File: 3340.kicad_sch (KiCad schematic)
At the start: 176 parts, among them J1 Conn_01x17, J10 FM1, J11 Conn_01x17, J12 V/OCT2, J13 PULSE2, J14 SAW2, J15 TRI2, J16 SINE2, J17 SYNC2, J18 Conn_01x17, J19 PWM2, J2 Conn_01x17, J20 FM2, J3 V/OCT1, J4 PULSE1, J5 SAW1, J6 TRI1, J7 SINE1, J8 SYNC1, J9 PWM1, Q1 2N3904, Q2 2N3906, Q3 2N3904, Q4 2N3906, Q5 2N3904, Q6 2N3904, SW2 DPDT_OOO, U1 TL072, U2 TL074, U3 CEM3340, U4 TL072, U5 CEM3340, U6 TL074

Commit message: Fix electrolytic footprints
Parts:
- C14, C15: footprint Capacitor_THT:C_Disc_D4.3mm_W1.9mm_P5.00mm -> Capacitor_THT:CP_Radial_D5.0mm_P2.00mm
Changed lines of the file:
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@@
       (effects (font (size 1.27 1.27)) (justify left))
     )
-    (property "Footprint" "Capacitor_THT:C_Disc_D4.3mm_W1.9mm_P5.00mm" (id 2) (at 61.9252 154.94 0)
+    (property "Footprint" "Capacitor_THT:CP_Radial_D5.0mm_P2.00mm" (id 2) (at 61.9252 154.94 0)
       (effects (font (size 1.27 1.27)) hide)
     )
@@
       (effects (font (size 1.27 1.27)) (justify left))
     )
-    (property "Footprint" "Capacitor_THT:C_Disc_D4.3mm_W1.9mm_P5.00mm" (id 2) (at 61.9252 172.72 0)
+    (property "Footprint" "Capacitor_THT:CP_Radial_D5.0mm_P2.00mm" (id 2) (at 61.9252 172.72 0)
       (effects (font (size 1.27 1.27)) hide)
     )
@@
     )
     (path "/4c10e0c8-c190-49b5-afef-1cfbf2c04b94"
-      (reference "C14") (unit 1) (value "10u") (footprint "Capacitor_THT:C_Disc_D4.3mm_W1.9mm_P5.00mm")
+      (reference "C14") (unit 1) (value "10u") (footprint "Capacitor_THT:CP_Radial_D5.0mm_P2.00mm")
     )
     (path "/575f3bf2-02c8-4aae-8013-f1397d2b5c57"
-      (reference "C15") (unit 1) (value "10u") (footprint "Capacitor_THT:C_Disc_D4.3mm_W1.9mm_P5.00mm")
+      (reference "C15") (unit 1) (value "10u") (footprint "Capacitor_THT:CP_Radial_D5.0mm_P2.00mm")
     )
     (path "/3a96b081-72fd-49bc-b6d2-c7dcd534bda7"

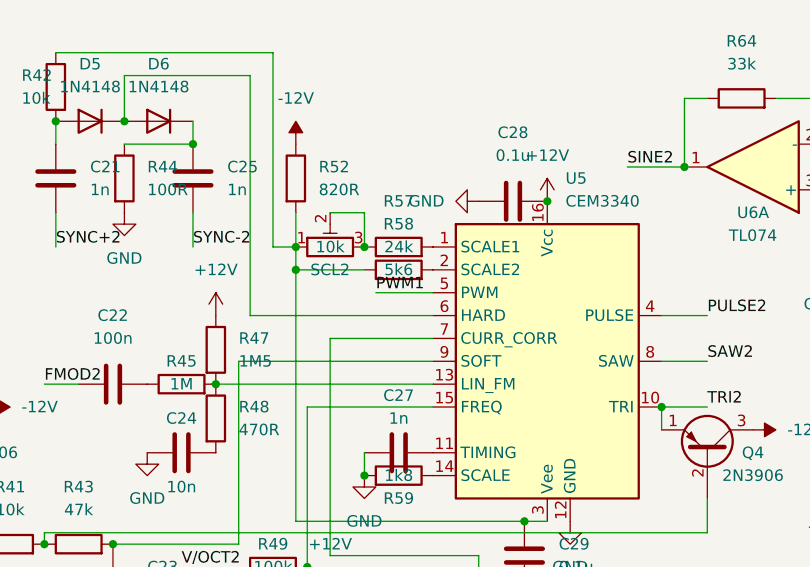
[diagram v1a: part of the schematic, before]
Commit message: Fix PWM2 connection
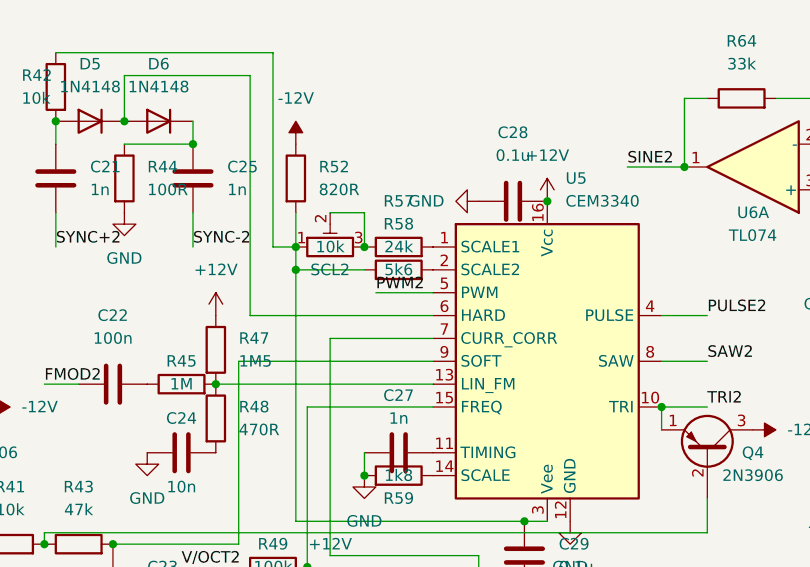
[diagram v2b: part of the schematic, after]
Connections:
- net PWM1: no longer U5.5 (PWM)
- net PWM2: now also U5.5 (PWM)
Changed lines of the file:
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@@
     (effects (font (size 1.27 1.27)) (justify left bottom))
   )
-  (label "PWM1" (at 157.48 43.18 0)
+  (label "PWM2" (at 157.48 43.18 0)
     (effects (font (size 1.27 1.27)) (justify left bottom))
   )

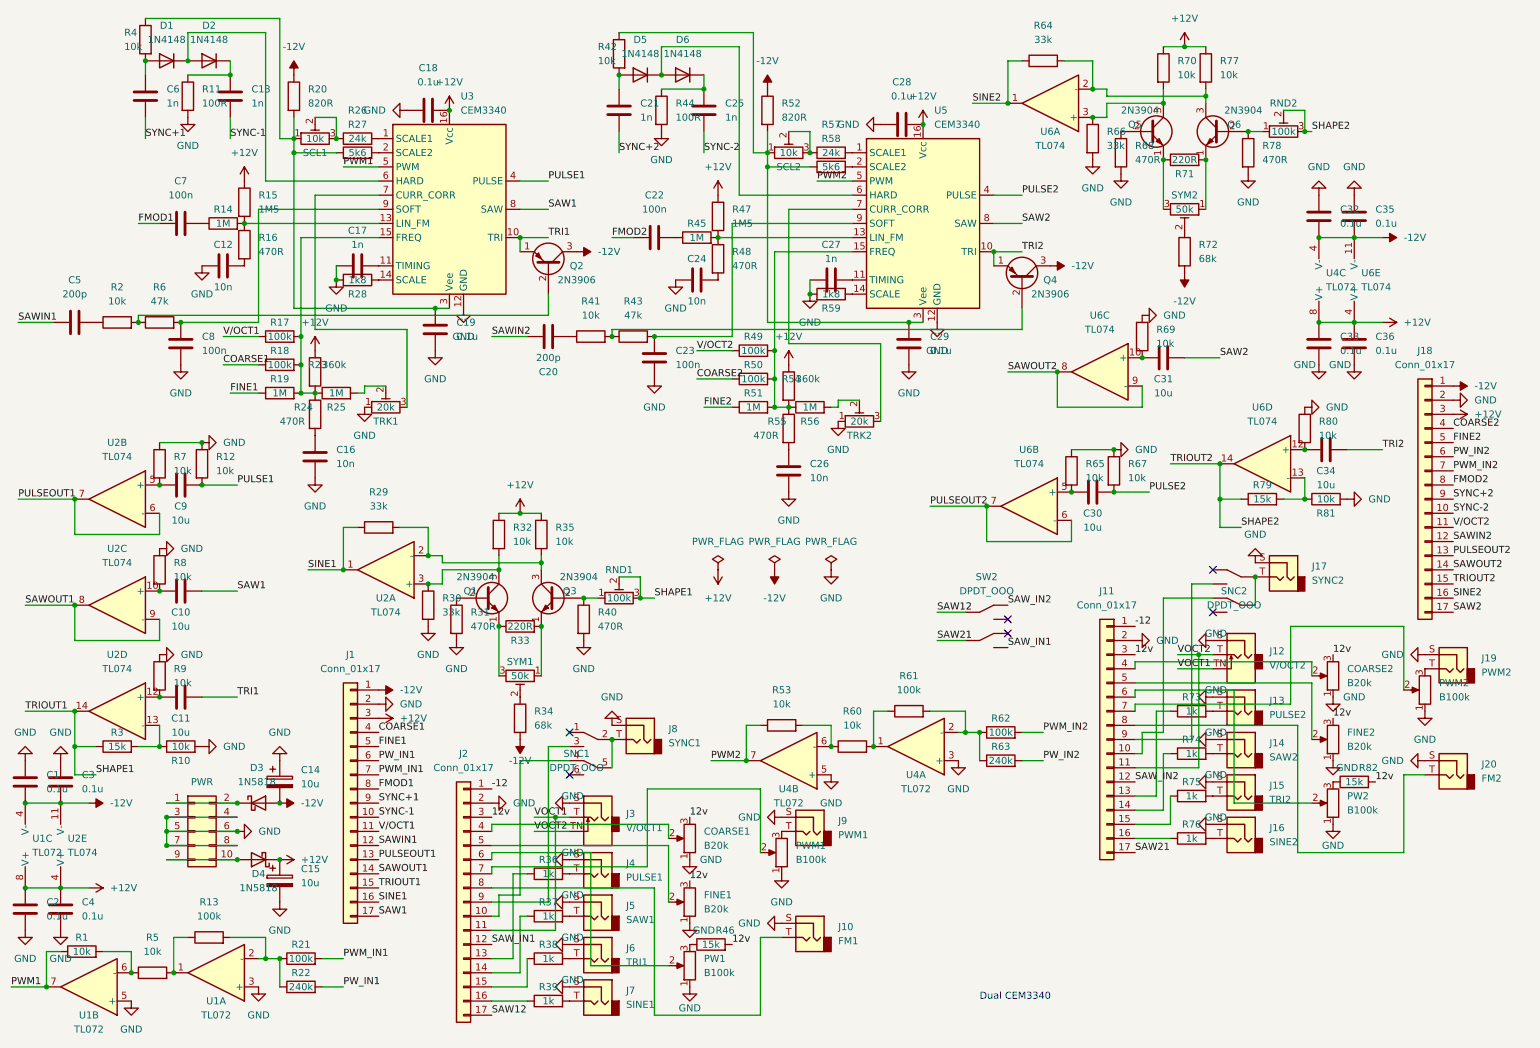
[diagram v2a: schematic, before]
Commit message: Add independent sync switches
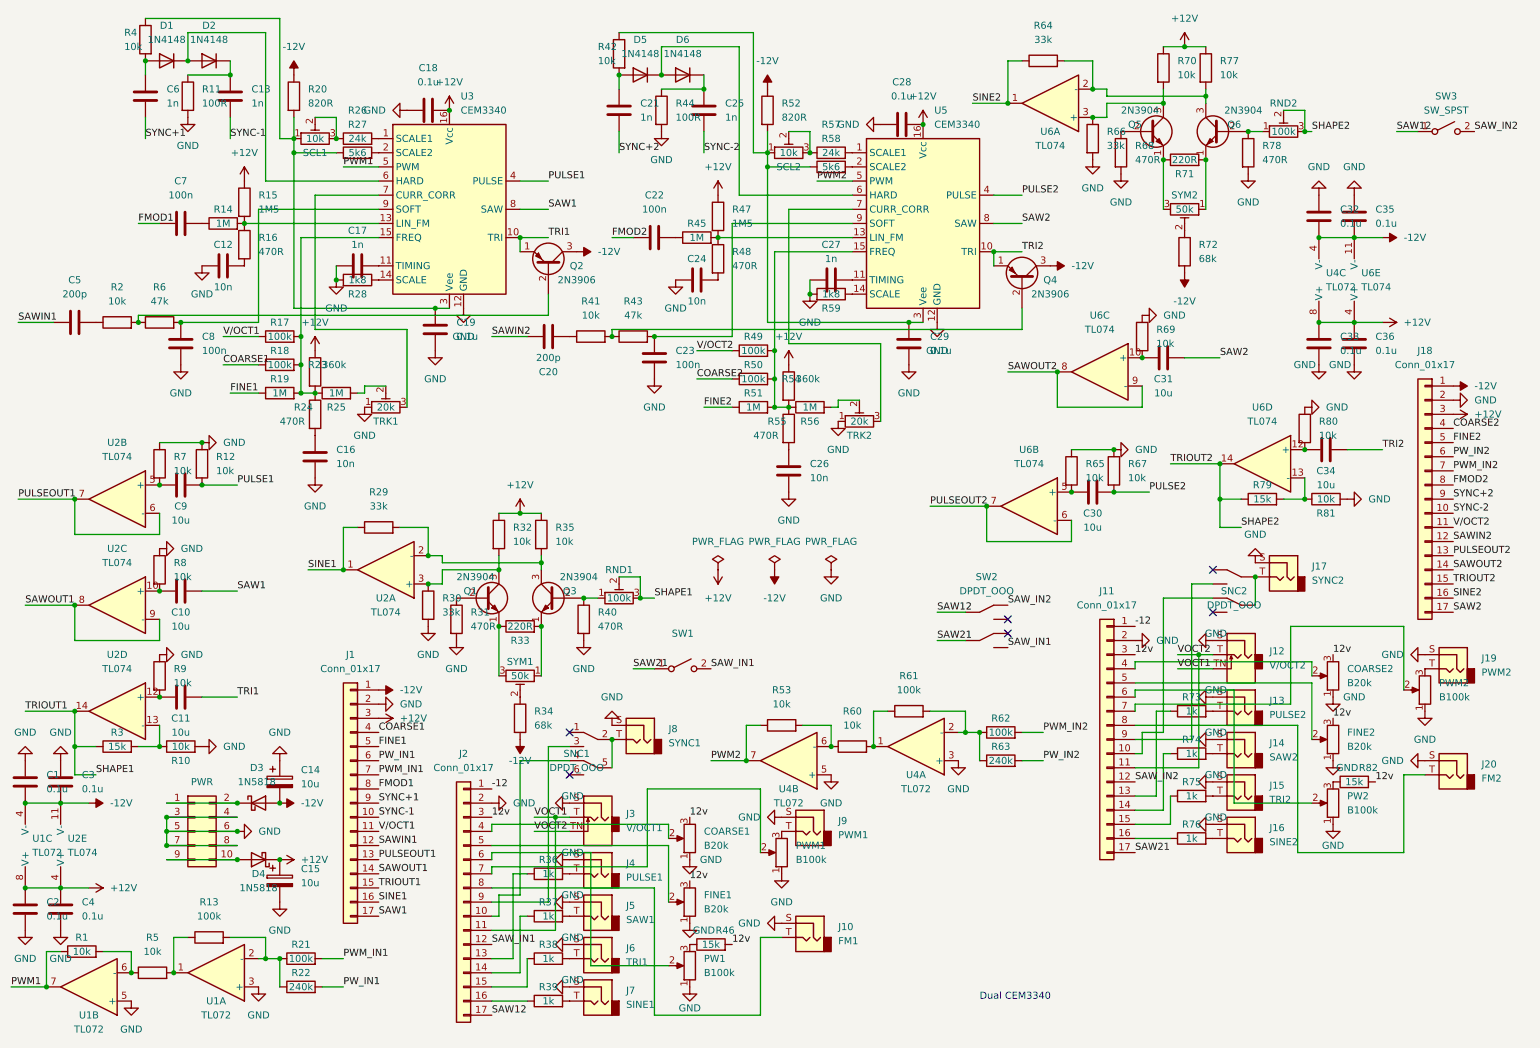
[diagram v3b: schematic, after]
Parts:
- added SW1: (no value), symbol Switch:SW_SPST
- added SW3: SW_SPST, symbol Switch:SW_SPST
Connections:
- net SAW12: now also SW3.1 (A)
- net SAW21: now also SW1.1 (A)
- net SAW_IN1: now also SW1.2 (B)
- net SAW_IN2: now also SW3.2 (B)
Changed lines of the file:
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@@
     (stroke (width 0) (type default) (color 0 0 0 0))
   )
+  (wire (pts (xy 261.62 34.29) (xy 265.43 34.29))
+    (stroke (width 0) (type default) (color 0 0 0 0))
+  )
   (wire (pts (xy 184.15 142.24) (xy 186.69 142.24))
     (stroke (width 0) (type default) (color 0 0 0 0))
@@
     (stroke (width 0) (type default) (color 0 0 0 0))
   )
+  (wire (pts (xy 124.46 130.81) (xy 128.27 130.81))
+    (stroke (width 0) (type default) (color 0 0 0 0))
+  )
   (wire (pts (xy 15.24 154.94) (xy 21.59 154.94))
     (stroke (width 0) (type default) (color 0 0 0 0))
@@
     (effects (font (size 1.27 1.27)) (justify left bottom))
   )
+  (label "SAW12" (at 261.62 34.29 0)
+    (effects (font (size 1.27 1.27)) (justify left bottom))
+  )
   (label "TRI1" (at 109.22 53.34 0)
     (effects (font (size 1.27 1.27)) (justify left bottom))
@@
     (effects (font (size 1.27 1.27)) (justify left bottom))
   )
+  (label "SAW_IN2" (at 275.59 34.29 0)
+    (effects (font (size 1.27 1.27)) (justify left bottom))
+  )
   (label "PWM2" (at 138.43 147.32 0)
     (effects (font (size 1.27 1.27)) (justify left bottom))
@@
     (effects (font (size 1.27 1.27)) (justify left bottom))
   )
+  (label "SAW21" (at 124.46 130.81 0)
+    (effects (font (size 1.27 1.27)) (justify left bottom))
+  )
   (label "SAW_IN1" (at 191.77 127 0)
     (effects (font (size 1.27 1.27)) (justify left bottom))
@@
     (effects (font (size 1.27 1.27)) (justify left bottom))
   )
+  (label "SAW_IN1" (at 138.43 130.81 0)
+    (effects (font (size 1.27 1.27)) (justify left bottom))
+  )
   (label "SAW2" (at 229.87 74.93 0)
     (effects (font (size 1.27 1.27)) (justify left bottom))
@@
     (pin "2")
     (pin "3")
+    (pin "5")
+    (pin "6")
+    (pin "7")
+    (pin "4")
+    (pin "8")
   )
   (symbol (lib_id "Device:R") (at 92.71 121.92 0) (unit 1)
@@
       (effects (font (size 1.27 1.27)) hide)
     )
+    (pin "1")
+    (pin "2")
+    (pin "3")
+    (pin "5")
+    (pin "6")
+    (pin "7")
     (pin "4")
     (pin "8")
@@
       (effects (font (size 1.27 1.27)) hide)
     )
+    (pin "1")
+    (pin "2")
+    (pin "3")
     (pin "5")
     (pin "6")
     (pin "7")
+    (pin "4")
+    (pin "8")
   )
   (symbol (lib_id "Device:R") (at 78.74 105.41 90) (unit 1)
@@
       (effects (font (size 1.27 1.27)) hide)
     )
+    (pin "1")
+    (pin "2")
+    (pin "3")
+    (pin "5")
+    (pin "6")
+    (pin "7")
     (pin "10")
     (pin "8")
     (pin "9")
+    (pin "12")
+    (pin "13")
+    (pin "14")
+    (pin "11")
+    (pin "4")
   )
   (symbol (lib_id "Device:R") (at 146.05 78.74 90) (unit 1)
@@
       (effects (font (size 1.27 1.27)) hide)
     )
+    (pin "1")
+    (pin "2")
+    (pin "3")
     (pin "5")
     (pin "6")
     (pin "7")
+    (pin "10")
+    (pin "8")
+    (pin "9")
+    (pin "12")
+    (pin "13")
+    (pin "14")
+    (pin "11")
+    (pin "4")
   )
   (symbol (lib_id "Device:C_Polarized") (at 60.96 151.13 0) (unit 1)
@@
     (pin "1")
   )
+  (symbol (lib_id "Switch:SW_SPST") (at 133.35 130.81 0) (unit 1)
+    (in_bom yes) (on_board yes) (fields_autoplaced)
+    (property "Reference" "SW1" (id 0) (at 133.35 124.46 0))
+    (property "Value" "" (id 1) (at 133.35 127 0))
+    (property "Footprint" "" (id 2) (at 133.35 130.81 0)
+      (effects (font (size 1.27 1.27)) hide)
+    )
+    (property "Datasheet" "~" (id 3) (at 133.35 130.81 0)
+      (effects (font (size 1.27 1.27)) hide)
+    )
+    (pin "1")
+    (pin "2")
+  )
   (symbol (lib_id "Device:C") (at 172.72 33.02 90) (unit 1)
     (in_bom yes) (on_board yes) (fields_autoplaced)
@@
       (effects (font (size 1.27 1.27)) hide)
     )
+    (pin "1")
+    (pin "2")
+    (pin "3")
+    (pin "5")
+    (pin "6")
+    (pin "7")
     (pin "4")
     (pin "8")
@@
     (pin "2")
     (pin "3")
+    (pin "5")
+    (pin "6")
+    (pin "7")
+    (pin "10")
+    (pin "8")
+    (pin "9")
+    (pin "12")
+    (pin "13")
+    (pin "14")
+    (pin "11")
+    (pin "4")
   )
   (symbol (lib_id "power:GND") (at 160.02 149.86 0) (unit 1)
@@
     (pin "2")
     (pin "3")
+    (pin "5")
+    (pin "6")
+    (pin "7")
+    (pin "4")
+    (pin "8")
   )
   (symbol (lib_id "power:-12V") (at 78.74 134.62 270) (unit 1)
@@
     (pin "1")
   )
+  (symbol (lib_id "Switch:SW_SPST") (at 270.51 34.29 0) (unit 1)
+    (in_bom yes) (on_board yes) (fields_autoplaced)
+    (property "Reference" "SW3" (id 0) (at 270.51 27.94 0))
+    (property "Value" "SW_SPST" (id 1) (at 270.51 30.48 0))
+    (property "Footprint" "" (id 2) (at 270.51 34.29 0)
+      (effects (font (size 1.27 1.27)) hide)
+    )
+    (property "Datasheet" "~" (id 3) (at 270.51 34.29 0)
+      (effects (font (size 1.27 1.27)) hide)
+    )
+    (pin "1")
+    (pin "2")
+  )
   (symbol (lib_id "Transistor_BJT:2N3906") (at 109.22 58.42 270) (mirror x) (unit 1)
     (in_bom yes) (on_board yes)
@@
       (effects (font (size 1.27 1.27)) hide)
     )
+    (pin "1")
+    (pin "2")
+    (pin "3")
+    (pin "5")
+    (pin "6")
+    (pin "7")
+    (pin "10")
+    (pin "8")
+    (pin "9")
+    (pin "12")
+    (pin "13")
+    (pin "14")
     (pin "11")
     (pin "4")
@@
       (effects (font (size 1.27 1.27)) hide)
     )
+    (pin "1")
+    (pin "2")
+    (pin "3")
     (pin "5")
     (pin "6")
     (pin "7")
+    (pin "4")
+    (pin "8")
   )
   (symbol (lib_id "Device:R") (at 25.4 181.61 90) (unit 1)
@@
     (pin "2")
     (pin "3")
+    (pin "5")
+    (pin "6")
+    (pin "7")
+    (pin "10")
+    (pin "8")
+    (pin "9")
+    (pin "12")
+    (pin "13")
+    (pin "14")
+    (pin "11")
+    (pin "4")
   )
   (symbol (lib_id "Device:D") (at 40.64 21.59 0) (mirror y) (unit 1)
@@
       (effects (font (size 1.27 1.27)) hide)
     )
+    (pin "1")
+    (pin "2")
+    (pin "3")
+    (pin "5")
+    (pin "6")
+    (pin "7")
+    (pin "10")
+    (pin "8")
+    (pin "9")
+    (pin "12")
+    (pin "13")
+    (pin "14")
     (pin "11")
     (pin "4")
@@
       (effects (font (size 1.27 1.27)) hide)
     )
+    (pin "1")
+    (pin "2")
+    (pin "3")
+    (pin "5")
+    (pin "6")
+    (pin "7")
+    (pin "10")
+    (pin "8")
+    (pin "9")
     (pin "12")
     (pin "13")
     (pin "14")
+    (pin "11")
+    (pin "4")
   )
   (symbol (lib_id "Connector:AudioJack2") (at 233.68 161.29 0) (mirror y) (unit 1)
@@
       (effects (font (size 1.27 1.27)) hide)
     )
+    (pin "1")
+    (pin "2")
+    (pin "3")
+    (pin "5")
+    (pin "6")
+    (pin "7")
     (pin "10")
     (pin "8")
     (pin "9")
+    (pin "12")
+    (pin "13")
+    (pin "14")
+    (pin "11")
+    (pin "4")
   )
   (symbol (lib_id "Device:R") (at 36.83 17.78 0) (mirror y) (unit 1)
@@
       (effects (font (size 1.27 1.27)) hide)
     )
+    (pin "1")
+    (pin "2")
+    (pin "3")
+    (pin "5")
+    (pin "6")
+    (pin "7")
+    (pin "10")
+    (pin "8")
+    (pin "9")
     (pin "12")
     (pin "13")
     (pin "14")
+    (pin "11")
+    (pin "4")
   )
   (symbol (lib_id "power:+12V") (at 26.67 170.18 270) (unit 1)
@@
       (effects (font (size 1.27 1.27)) hide)
     )
+    (pin "1")
+    (pin "2")
+    (pin "3")
     (pin "5")
     (pin "6")
     (pin "7")
+    (pin "10")
+    (pin "8")
+    (pin "9")
+    (pin "12")
+    (pin "13")
+    (pin "14")
+    (pin "11")
+    (pin "4")
   )
   (symbol (lib_id "Device:R") (at 67.31 77.47 0) (unit 1)
@@
       (reference "SNC2") (unit 1) (value "DPDT_OOO") (footprint "Button_Switch_THT:SW_DPDT_Toggle_Miniature_Lug")
     )
+    (path "/4f77388d-b9d0-4512-8c08-99b0c79a19a3"
+      (reference "SW1") (unit 1) (value "SW_SPST") (footprint "")
+    )
     (path "/ca8492c6-a762-403e-a1f8-477330a423ed"
       (reference "SW2") (unit 1) (value "DPDT_OOO") (footprint "Button_Switch_THT:SW_DPDT_Toggle_Miniature_Lug")
     )
+    (path "/8e0d0ff3-73a6-4f79-ba76-e56792c0dc09"
+      (reference "SW3") (unit 1) (value "SW_SPST") (footprint "")
+    )
     (path "/54012768-bb14-48fe-ad71-d0399b5b51ab"
